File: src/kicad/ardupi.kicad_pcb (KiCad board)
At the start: 2 copper layers, 65 x 30 mm, 57 parts, among them J1 GPIO_CONNECTOR, J10 TSW-108-08-L-T-RA, J2 Conn_01x10, J3 Conn_01x05, J4 Conn_01x04, J5 Conn_01x05, J6 Conn_01x06, J7 Conn_01x04, J8 Conn_01x02, J9 Conn_01x04, U1 MPU-9250, U2 ULN2803ADW, U4 PCA9685BS, U6 ADS1115IRUGR

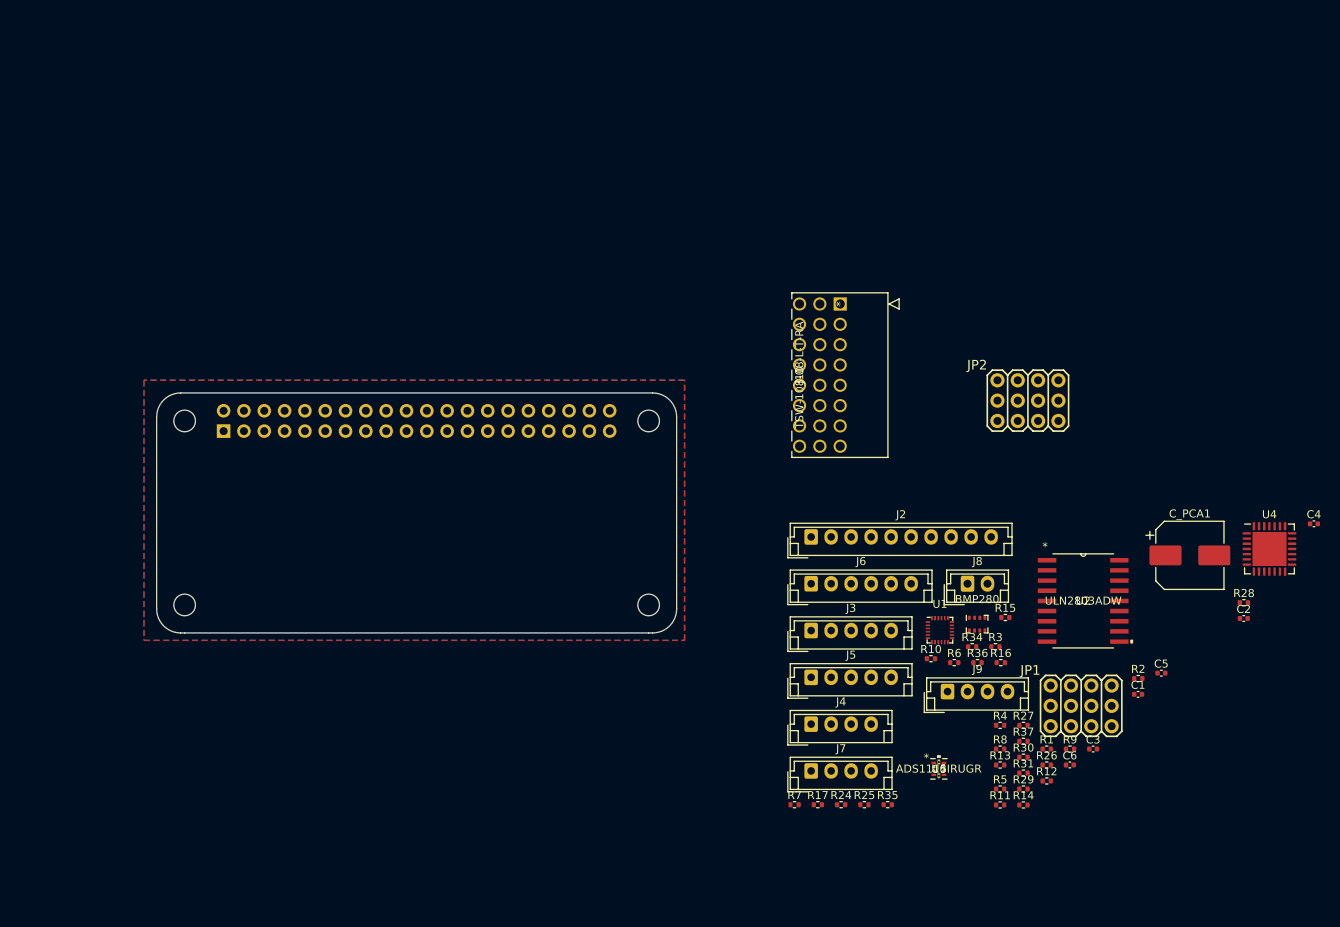
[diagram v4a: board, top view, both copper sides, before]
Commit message: +HAT ID EEPROM +standard rpi-4b footprint +clean up of schematic
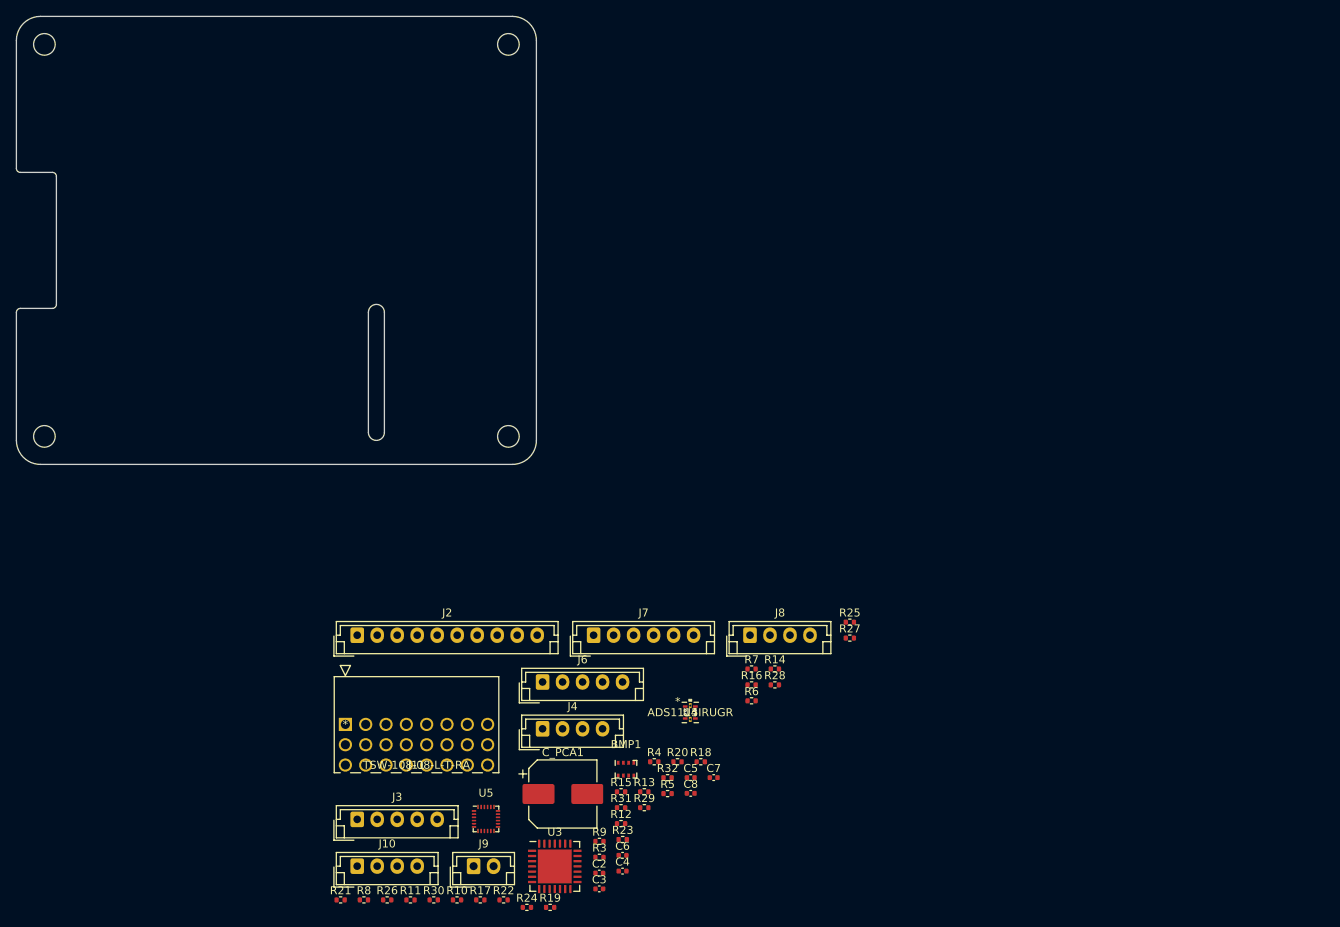
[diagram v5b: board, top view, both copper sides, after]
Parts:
- removed BMP280: BMP280, Package_LGA:Bosch_LGA-8_2x2.5mm_P0.65mm_ClockwisePinNumbering
- removed C1: 0.1uF, Capacitor_SMD:C_0402_1005Metric
- removed H1, H2, H3, H4: MountingHole, lib:MountingHole_2.7mm_M2.5_uHAT_RPi
- removed J1: GPIO_CONNECTOR, lib:PinSocket_2x20_P2.54mm_Vertical_Centered_Anchor
- removed J5: Conn_01x05, Connector_JST:JST_EH_B5B-EH-A_1x05_P2.50mm_Vertical
- removed JP1, JP2: PWM-HEADER-3X04, Ardupi:PWM-Header-3x4
- removed R1: 10K, Resistor_SMD:R_0402_1005Metric
- removed R2: 10k, Resistor_SMD:R_0402_1005Metric
- removed R34, R35, R36, R37: 10KΩ, Resistor_SMD:R_0402_1005Metric
- removed U1: MPU-9250, Sensor_Motion:InvenSense_QFN-24_3x3mm_P0.4mm
- removed U2: ULN2803ADW, uln2803ADW:ULN2803ADW
- removed U6: ADS1115IRUGR, Ardupi:ADS1115IRUGR
- added BMP1: BMP280, Package_LGA:Bosch_LGA-8_2x2.5mm_P0.65mm_ClockwisePinNumbering, F.Cu at (176.2, 138.1)
- added C7: 0.01uF, Capacitor_SMD:C_0402_1005Metric, F.Cu at (187.2, 139.2)
- added C8: 1uF, Capacitor_SMD:C_0402_1005Metric, F.Cu at (184.3, 141.1)
- added J11: TSW-108-08-L-T-RA, Ardupi:TSW-108-08-L-T-RA, F.Cu at (141.1, 132.5)
- added MH1: MountingHole_2.7mm_M2.5, MountingHole:MountingHole_2.7mm_M2.5, F.Cu at (103.5, 47.5)
- added MH2: MountingHole_2.7mm_M2.5, MountingHole:MountingHole_2.7mm_M2.5, F.Cu at (161.5, 47.5)
- added MH3: MountingHole_2.7mm_M2.5, MountingHole:MountingHole_2.7mm_M2.5, F.Cu at (103.5, 96.5)
- added MH4: MountingHole_2.7mm_M2.5, MountingHole:MountingHole_2.7mm_M2.5, F.Cu at (161.5, 96.5)
- added R18: 220 Ω, Resistor_SMD:R_0402_1005Metric, F.Cu at (185.6, 137.2)
- added R19: 220 Ω, Resistor_SMD:R_0402_1005Metric, F.Cu at (166.7, 155.4)
- added R20: 220 Ω, Resistor_SMD:R_0402_1005Metric, F.Cu at (182.6, 137.2)
- added R21: 4.7KΩ, Resistor_SMD:R_0402_1005Metric, F.Cu at (140.5, 154.4)
- added R22: 4.7KΩ, Resistor_SMD:R_0402_1005Metric, F.Cu at (160.9, 154.4)
- added R23: 10KΩ, Resistor_SMD:R_0402_1005Metric, F.Cu at (175.8, 146.9)
- added R32: 10KΩ, Resistor_SMD:R_0402_1005Metric, F.Cu at (181.4, 139.2)
- added U3: PCA9685BS, Package_DFN_QFN:QFN-28-1EP_6x6mm_P0.65mm_EP4.25x4.25mm, F.Cu at (167.3, 150.2)
- added U5: MPU-9250, Sensor_Motion:InvenSense_QFN-24_3x3mm_P0.4mm, F.Cu at (158.7, 144.3)
- C2: value 1uF -> 0.1uF
- C3: value 0.1uF -> 1uF
- C4: value 0.01uF -> 1uF
- C5: value 1uF -> 0.1uf
- C6: value 10uF -> 0.1uF
- J10: value TSW-108-08-L-T-RA -> Conn_01x04; footprint Ardupi:TSW-108-08-L-T-RA -> Connector_JST:JST_EH_B4B-EH-A_1x04_P2.50mm_Vertical
- J6: value Conn_01x06 -> Conn_01x05; footprint Connector_JST:JST_EH_B6B-EH-A_1x06_P2.50mm_Vertical -> Connector_JST:JST_EH_B5B-EH-A_1x05_P2.50mm_Vertical
- J7: value Conn_01x04 -> Conn_01x06; footprint Connector_JST:JST_EH_B4B-EH-A_1x04_P2.50mm_Vertical -> Connector_JST:JST_EH_B6B-EH-A_1x06_P2.50mm_Vertical
- J8: value Conn_01x02 -> Conn_01x04; footprint Connector_JST:JST_EH_B2B-EH-A_1x02_P2.50mm_Vertical -> Connector_JST:JST_EH_B4B-EH-A_1x04_P2.50mm_Vertical
- J9: value Conn_01x04 -> Conn_01x02; footprint Connector_JST:JST_EH_B4B-EH-A_1x04_P2.50mm_Vertical -> Connector_JST:JST_EH_B2B-EH-A_1x02_P2.50mm_Vertical
- R10: value 220 Ω -> 10k
- R11: value 220 Ω -> 10K
- R12: value 220 Ω -> 460
- R25, R27, R30: value 4.7KΩ -> 10KΩ
- R28: value 10KΩ -> 4.7KΩ
- R3, R4, R5: value 10K -> 10k
- R6, R7: value 10k -> 10K
- R8: value 470k -> 10K
- R9: value 470k -> 10k
- U4: value PCA9685BS -> ADS1115IRUGR; footprint Package_DFN_QFN:QFN-28-1EP_6x6mm_P0.65mm_EP4.25x4.25mm -> Ardupi:ADS1115IRUGR
- moved C4 96.7 mm to (175.8, 150.8)
- moved J10 92.6 mm to (142.6, 150.2), turned to 0 degrees
- moved C2 86.6 mm to (172.9, 151.1)
- moved R26 84.1 mm to (146.3, 154.4)
- moved C_PCA1 83.9 mm to (168.3, 141.2)
- moved R8 81.7 mm to (143.4, 154.4)
- moved R30 75.8 mm to (152.2, 154.4)
- moved U4 75.2 mm to (184.2, 131.0)
- moved R11 74.7 mm to (149.3, 154.4)
- moved R10 66.5 mm to (155.1, 154.4)
- moved C3 64.2 mm to (172.9, 153.1)
- moved J9 63.1 mm to (157.2, 150.2)
- moved J3 61.5 mm to (142.6, 144.4)
- moved C5 60.3 mm to (184.3, 139.2)
- moved R9 59.9 mm to (172.9, 147.1)
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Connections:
- C3 pad 1: Net-(C3-Pad1) -> /+3.3V
- C4 pad 1: /+3.3V -> +5V
- C5 pad 1: /+3.3V -> +5V
- J10 pad 1: unconnected-(J10-Pad1) -> +5V
- J10 pad 2: unconnected-(J10-Pad2) -> /SDA
- J10 pad 3: unconnected-(J10-Pad3) -> /SCL
- J10 pad 4: unconnected-(J10-Pad4) -> GND
- J6 pad 1: /AIO3 -> /BUZZER_OUT
- J6 pad 2: /AIO2 -> /LED1_OUT
- J6 pad 3: /AIO1 -> /LED2_OUT
- J6 pad 4: /AIO0 -> /LED3_OUT
- J6 pad 5: GND -> V_EXT
- J7 pad 1: +5V -> /AIO3
- J7 pad 2: /SDA -> /AIO2
- J7 pad 3: /SCL -> /AIO1
- J7 pad 4: GND -> /AIO0
- J8 pad 1: /SRVO_EN -> +5V
- J8 pad 2: Net-(J8-Pad2) -> /SDA
- J9 pad 1: +5V -> /SRVO_EN
- J9 pad 2: /SDA -> Net-(J9-Pad2)
- R10 pad 2: /PWM1 -> GND
- R11 pad 1: Net-(JP1-Pad4) -> +5V
- R11 pad 2: /PWM2 -> Net-(J9-Pad2)
- R12 pad 1: Net-(JP1-Pad7) -> /PCA_EN
- R12 pad 2: /PWM3 -> Net-(J9-Pad2)
- R13 pad 2: /PWM4 -> /PWM1
- R14 pad 2: /PWM5 -> /PWM2
- R15 pad 2: /PWM6 -> /PWM3
- R16 pad 2: /PWM7 -> /PWM4
- R17 pad 1: Net-(JP2-Pad10) -> /PWM8
- R17 pad 2: /PWM8 -> Net-(J11-Pad22)
- R24 pad 2: /SPI_SCLK -> /SPI_CE1_N
- R25 pad 1: /+3.3V -> Net-(R25-Pad1)
- R25 pad 2: /SPI_MOSI -> +5V
- R26 pad 1: GND -> /SPI_CE0_N
- R26 pad 2: /SPI_MISO -> /+3.3V
- R27 pad 1: /+3.3V -> Net-(R27-Pad1)
- R27 pad 2: /SPI_CE1_N -> +5V
- R28 pad 1: /SPI_CE0_N -> /SPI_SCLK
- R29 pad 1: /SPI_SCLK -> /SPI_MOSI
- R3 pad 1: Net-(R3-Pad1) -> +5V
- R3 pad 2: GND -> /SDA1
- R30 pad 1: /SPI_MOSI -> /SPI_MISO
- R30 pad 2: /+3.3V -> GND
- R31 pad 1: /SPI_MISO -> /SCL1
- R31 pad 2: GND -> +5V
- R4 pad 1: Net-(R4-Pad1) -> +5V
- R4 pad 2: GND -> /SCL1
- R8 pad 1: +5V -> Net-(R8-Pad1)
- R8 pad 2: Net-(J8-Pad2) -> GND
- R9 pad 1: /PCA_EN -> Net-(R9-Pad1)
- R9 pad 2: Net-(J8-Pad2) -> GND
- U4 pad 1: Net-(R5-Pad1) -> Net-(R27-Pad1)
- U4 pad 10: /PWM8 -> /SCL1
- U4 pad 4: /PWM2 -> /AIO0
- U4 pad 5: /PWM3 -> /AIO1
- U4 pad 6: /PWM4 -> /AIO2
- U4 pad 9: /PWM7 -> /SDA1
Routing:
- removed copper zone on B.Cu, net GND
- removed copper zone on F.Cu, net GND
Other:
- board size 65 x 30 mm -> 65 x 56 mm
- rule pad_to_mask_clearance: 0.051 -> 0
- board text added: "CAMERA (OPTIONAL)"
- board text added: "DISPLAY (OPTIONAL)"
- board text added: "Extend PCB edge 0.5mm if using SMT header"
- board text added: "PoE"
- board text added: "RJ45"
- board text added: "USB"
- board text removed: "Board Corner Radius = 3mm All holes are M2.5"
- board text removed: "Board dimensions are on Cmts (Comments) layer. Deselect it in Layers Manager to make them invisible. GPIO connector nets are not connected, these will get updated as per your schematic/netlist."

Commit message: - created ardupi parts library. - kicad parts should be completely sorted now, easy to add new parts. - added datasheets for supported ardupilot sensors
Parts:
- removed BMP1: BMP280, Package_LGA:Bosch_LGA-8_2x2.5mm_P0.65mm_ClockwisePinNumbering
- removed R21, R22, R24: 4.7KΩ, Resistor_SMD:R_0402_1005Metric
- removed R23: 10KΩ, Resistor_SMD:R_0402_1005Metric
- added R33: 4.7KΩ, Resistor_SMD:R_0402_1005Metric, F.Cu at (247.3, 110.2)
- added R34: 4.7KΩ, Resistor_SMD:R_0402_1005Metric, F.Cu at (264.6, 72.1)
- added R35: 4.7KΩ, Resistor_SMD:R_0402_1005Metric, F.Cu at (247.3, 97.5)
- added R36: 10KΩ, Resistor_SMD:R_0402_1005Metric, F.Cu at (232.1, 97.5)
- added U1: CAT24C256, Ardupi:CAT24C256HU4IGT3, F.Cu at (44.1, 64.4)
- added U2: ULN2803ADW, Ardupi:ULN2803ADWR, F.Cu at (209.2, 31.4)
- added U6: BMP280, Ardupi:bmp280, F.Cu at (201.6, 97.5)
- R28: value 4.7KΩ -> 10KΩ
- R30: value 10KΩ -> 4.7KΩ
- U3: footprint Package_DFN_QFN:QFN-28-1EP_6x6mm_P0.65mm_EP4.25x4.25mm -> Ardupi:PCA9685BS_118
- U4: footprint Ardupi:ADS1115IRUGR -> Ardupi:ADS1115IRUGT
- U5: footprint Sensor_Motion:InvenSense_QFN-24_3x3mm_P0.4mm -> Ardupi:mpu9250
- moved J11 202.7 mm to (343.8, 135.6)
- moved R6 170.8 mm to (34.0, 64.4)
- moved R9 160.7 mm to (34.0, 66.4)
- moved J8 157.4 mm to (41.5, 168.3)
- moved R30 155.9 mm to (282.9, 69.5)
- moved R10 148.6 mm to (36.9, 64.4)
- moved J9 144.3 mm to (300.7, 135.3)
- moved J7 133.5 mm to (39.0, 130.2)
- moved R11 132.5 mm to (280.3, 135.3)
- moved J4 132.3 mm to (41.5, 178.4)
- moved C6 124.7 mm to (277.8, 77.1)
- moved J6 122.1 mm to (234.6, 26.3), turned to -90 degrees
- moved R17 115.7 mm to (273.1, 142.9)
- moved R20 111.2 mm to (293.0, 150.5)
- moved J2 105.1 mm to (41.6, 150.5)
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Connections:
- C2 pad 1: /+3.3V -> +3V3
- C3 pad 1: /+3.3V -> +3V3
- C7 pad 1: /+3.3V -> +3V3
- C8 pad 1: /+3.3V -> +3V3
- R10 pad 1: Net-(R10-Pad1) -> unconnected-(R10-Pad1)
- R26 pad 1: /SPI_CE0_N -> /SPI_MISO
- R26 pad 2: /+3.3V -> GND
- R28 pad 1: /SPI_SCLK -> /SPI_MOSI
- R28 pad 2: /+3.3V -> +3V3
- R29 pad 1: /SPI_MOSI -> /SPI_SCLK
- R29 pad 2: /+3.3V -> +3V3
- R30 pad 1: /SPI_MISO -> /SPI_CE0_N
- R30 pad 2: GND -> +3V3
- R5 pad 1: Net-(R5-Pad1) -> unconnected-(R5-Pad1)
- R6 pad 1: Net-(R6-Pad1) -> unconnected-(R6-Pad1)
- R9 pad 1: Net-(R9-Pad1) -> unconnected-(R9-Pad1)
- U3 pad 1: Net-(R8-Pad1) -> unconnected-(U3-Pad1)
- U3 pad 10: /PWM8 -> /PWM7
- U3 pad 12: /PWM9 -> /PWM8
- U3 pad 13: /PWM10 -> /PWM9
- U3 pad 14: /PWM11 -> /PWM10
- U3 pad 15: /PWM12 -> /PWM11
- U3 pad 16: /PWM13 -> /PWM12
- U3 pad 17: /PWM14 -> /PWM13
- U3 pad 18: /PWM15 -> /PWM14
- U3 pad 19: /PWM16 -> /PWM15
- U3 pad 2: Net-(R9-Pad1) -> unconnected-(U3-Pad2)
- U3 pad 20: /PCA_EN -> unconnected-(U3-Pad20)
- U3 pad 21: Net-(R10-Pad1) -> unconnected-(U3-Pad21)
- U3 pad 22: GND -> /SCL1
- U3 pad 23: /SDA1 -> Net-(R7-Pad1)
- U3 pad 24: /SCL1 -> Net-(R8-Pad1)
- U3 pad 25: +5V -> unconnected-(U3-Pad25)
- U3 pad 26: Net-(R5-Pad1) -> /PCA_EN
- U3 pad 27: Net-(R6-Pad1) -> unconnected-(U3-Pad27)
- U3 pad 28: Net-(R7-Pad1) -> unconnected-(U3-Pad28)
- U3 pad 3: /PWM1 -> unconnected-(U3-Pad3)
- U3 pad 4: /PWM2 -> /PWM1
- U3 pad 5: /PWM3 -> /PWM2
- U3 pad 6: /PWM4 -> /PWM3
- U3 pad 7: /PWM5 -> /PWM4
- U3 pad 8: /PWM6 -> /PWM5
- U3 pad 9: /PWM7 -> /PWM6
- U5 pad 13: /+3.3V -> +3V3
- U5 pad 14: (no net) -> unconnected-(U5-Pad14)
- U5 pad 15: (no net) -> unconnected-(U5-Pad15)
- U5 pad 16: (no net) -> unconnected-(U5-Pad16)
- U5 pad 17: (no net) -> unconnected-(U5-Pad17)
- U5 pad 18: GND -> unconnected-(U5-Pad18)
- U5 pad 19: (no net) -> unconnected-(U5-Pad19)
- U5 pad 2: (no net) -> unconnected-(U5-Pad2)
- U5 pad 3: (no net) -> unconnected-(U5-Pad3)
- U5 pad 4: (no net) -> unconnected-(U5-Pad4)
- U5 pad 5: (no net) -> unconnected-(U5-Pad5)
- U5 pad 6: (no net) -> unconnected-(U5-Pad6)
- U5 pad 8: /+3.3V -> +3V3

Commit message: Basic pcb layout
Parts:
- added J1: Conn_01x02, Connector_JST:JST_EH_B2B-EH-A_1x02_P2.50mm_Vertical, F.Cu at (21.3, 23.8)
- moved J11 322.7 mm to (21.3, 143.2), turned to 90 degrees
- moved J9 283.1 mm to (18.7, 110.2), turned to 90 degrees
- moved R11 232.1 mm to (51.7, 94.9)
- moved R20 219.9 mm to (74.6, 125.4)
- moved J6 214.3 mm to (21.3, 46.6), turned to 90 degrees
- moved R12 206.7 mm to (64.4, 115.2)
- moved R31 206.7 mm to (64.4, 122.9)
- moved R7 206.7 mm to (64.4, 118.9)
- moved R17 206.7 mm to (67.3, 122.9)
- moved R14 197.1 mm to (79.7, 140.6)
- moved R16 197.1 mm to (71.0, 142.7)
- moved R18 197.1 mm to (68.0, 142.7)
- moved R19 197.1 mm to (71.0, 140.7)
- moved R13 167.7 mm to (82.2, 145.7)
- moved R15 166.1 mm to (77.1, 150.5)
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
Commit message: fix layout
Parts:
- removed R10, R5, R9: 10k, Resistor_SMD:R_0402_1005Metric
- removed R6: 10K, Resistor_SMD:R_0402_1005Metric
- J1: value Conn_01x02 -> GPIO; footprint Connector_JST:JST_EH_B2B-EH-A_1x02_P2.50mm_Vertical -> Connector_PinSocket_2.54mm:PinSocket_2x20_P2.54mm_Vertical; moved to B.Cu
- moved J2 155.9 mm to (161.3, 82.0), turned to 90 degrees
- moved J4 135.0 mm to (117.2, 87.4), turned to 90 degrees
- moved J8 120.8 mm to (107.3, 87.3), turned to 90 degrees
- moved J10 117.3 mm to (112.3, 87.3), turned to 90 degrees
- moved R8 115.0 mm to (119.1, 51.9), turned to 90 degrees
- moved J6 110.9 mm to (119.8, 97.4), turned to 180 degrees
- moved J7 110.4 mm to (128.2, 97.0), turned to 0 degrees
- moved J11 109.2 mm to (106.3, 74.7)
- moved J9 102.2 mm to (103.2, 52.6), turned to 0 degrees
- moved R15 99.2 mm to (114.5, 58.6)
- moved U4 98.2 mm to (142.2, 92.4)
- moved R13 96.4 mm to (114.5, 54.9)
- moved R18 96.0 mm to (120.8, 62.5), turned to -90 degrees
- moved R16 93.1 mm to (114.5, 60.4)
- moved R19 92.0 mm to (119.3, 62.4), turned to -90 degrees
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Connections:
- J1 pad 1: V_EXT -> +3V3
- J1 pad 2: Net-(BT1-Pad2) -> +5V
- U1 pad 4: unconnected-(U1-Pad4) -> GND
- U1 pad 5: unconnected-(U1-Pad5) -> /ID_SDA
- U1 pad 6: unconnected-(U1-Pad6) -> /ID_SCL
- U1 pad 7: unconnected-(U1-Pad7) -> /ID_SCL
- U1 pad 8: unconnected-(U1-Pad8) -> +3V3
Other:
- outline, holes or cut-outs redrawn
- board text removed: "DISPLAY (OPTIONAL)"
